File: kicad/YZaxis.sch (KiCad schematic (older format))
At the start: 34 parts, among them CON16 YZ, CON17 Stepstick_Left_Connector, CON18 Stepstick_Right_Connector, CON19 Stepstick_Left_Connector, CON20 Stepstick_Right_Connector, Q5 IRLR2905ZPBF, Q6 FDC6401N, U1 CD4504BPW

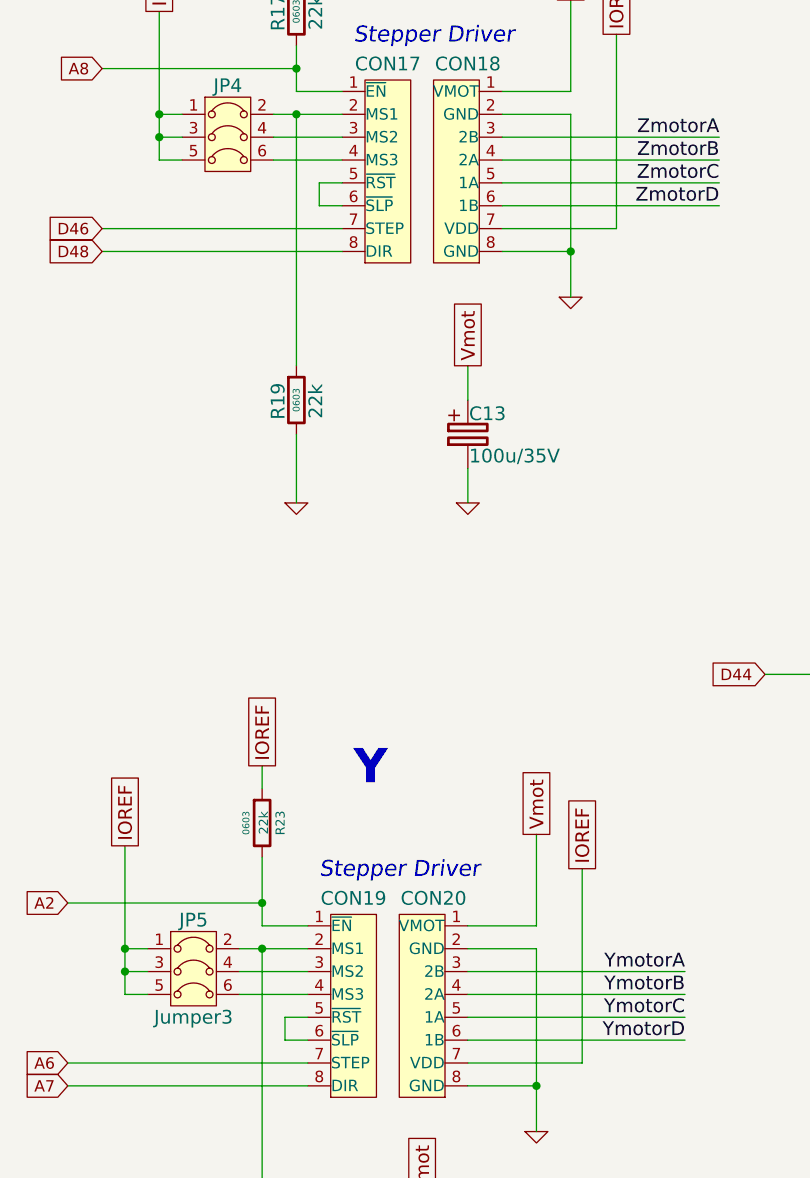
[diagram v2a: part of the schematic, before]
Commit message: Add footprint informations
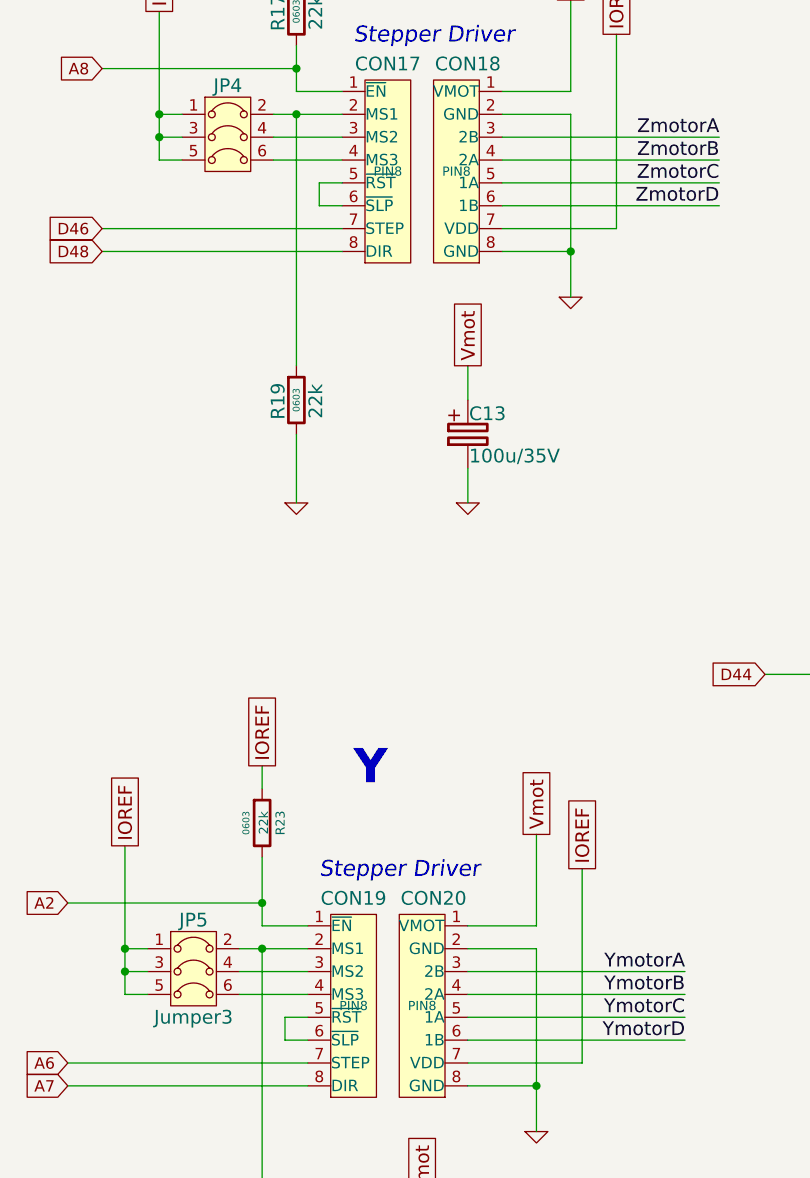
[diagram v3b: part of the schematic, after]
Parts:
- CON17, CON18, CON19, CON20: footprint (none) -> PIN8
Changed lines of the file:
@@
 F 0 "CON19" H 2400 6170 60  0000 C CNN
 F 1 "Stepstick_Left_Connector" H 2400 5250 60  0001 C CNN
-F 2 "" H 2400 5700 40  0000 C CNN
+F 2 "PIN8" H 2400 5700 40  0000 C CNN
 F 3 "" H 2400 5700 40  0000 C CNN
 	1    2400 5700
@@
 F 0 "CON20" H 2750 6170 60  0000 C CNN
 F 1 "Stepstick_Right_Connector" H 2750 5250 60  0001 C CNN
-F 2 "" H 2700 5700 40  0000 C CNN
+F 2 "PIN8" H 2700 5700 40  0000 C CNN
 F 3 "" H 2700 5700 40  0000 C CNN
 	1    2750 5700
@@
 F 0 "CON17" H 2550 2520 60  0000 C CNN
 F 1 "Stepstick_Left_Connector" H 2550 1600 60  0001 C CNN
-F 2 "" H 2550 2050 40  0000 C CNN
+F 2 "PIN8" H 2550 2050 40  0000 C CNN
 F 3 "" H 2550 2050 40  0000 C CNN
 	1    2550 2050
@@
 F 0 "CON18" H 2900 2520 60  0000 C CNN
 F 1 "Stepstick_Right_Connector" H 2900 1600 60  0001 C CNN
-F 2 "" H 2850 2050 40  0000 C CNN
+F 2 "PIN8" H 2850 2050 40  0000 C CNN
 F 3 "" H 2850 2050 40  0000 C CNN
 	1    2900 2050

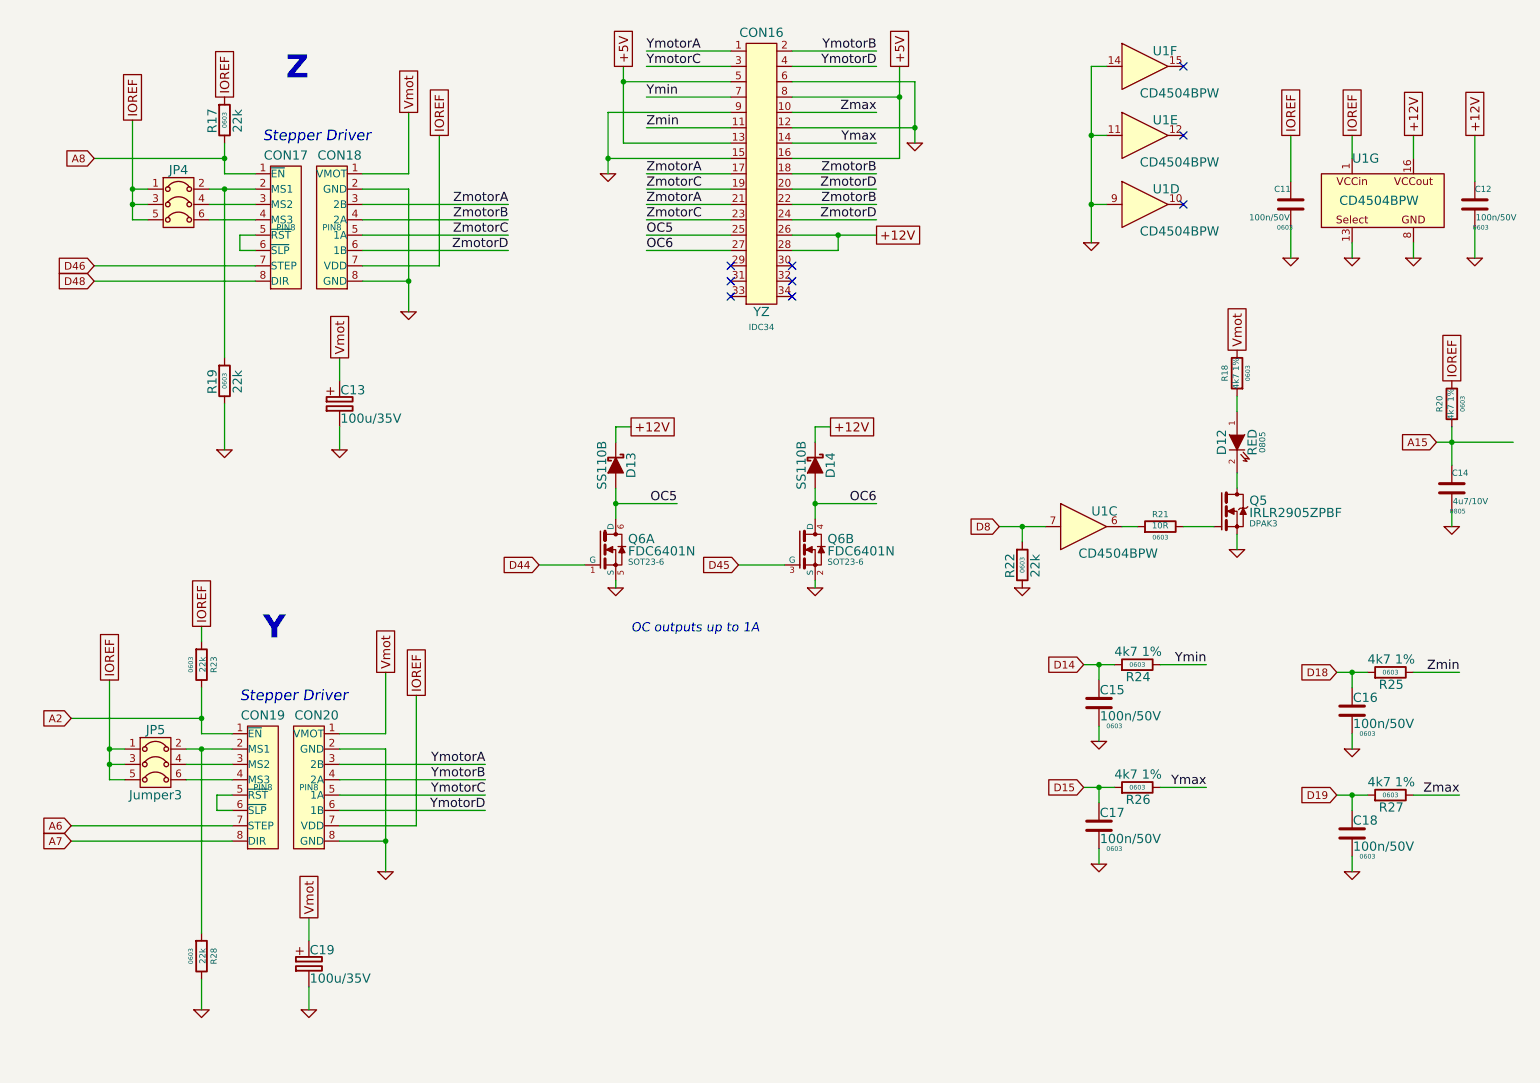
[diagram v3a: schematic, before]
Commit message: Add footprint informations
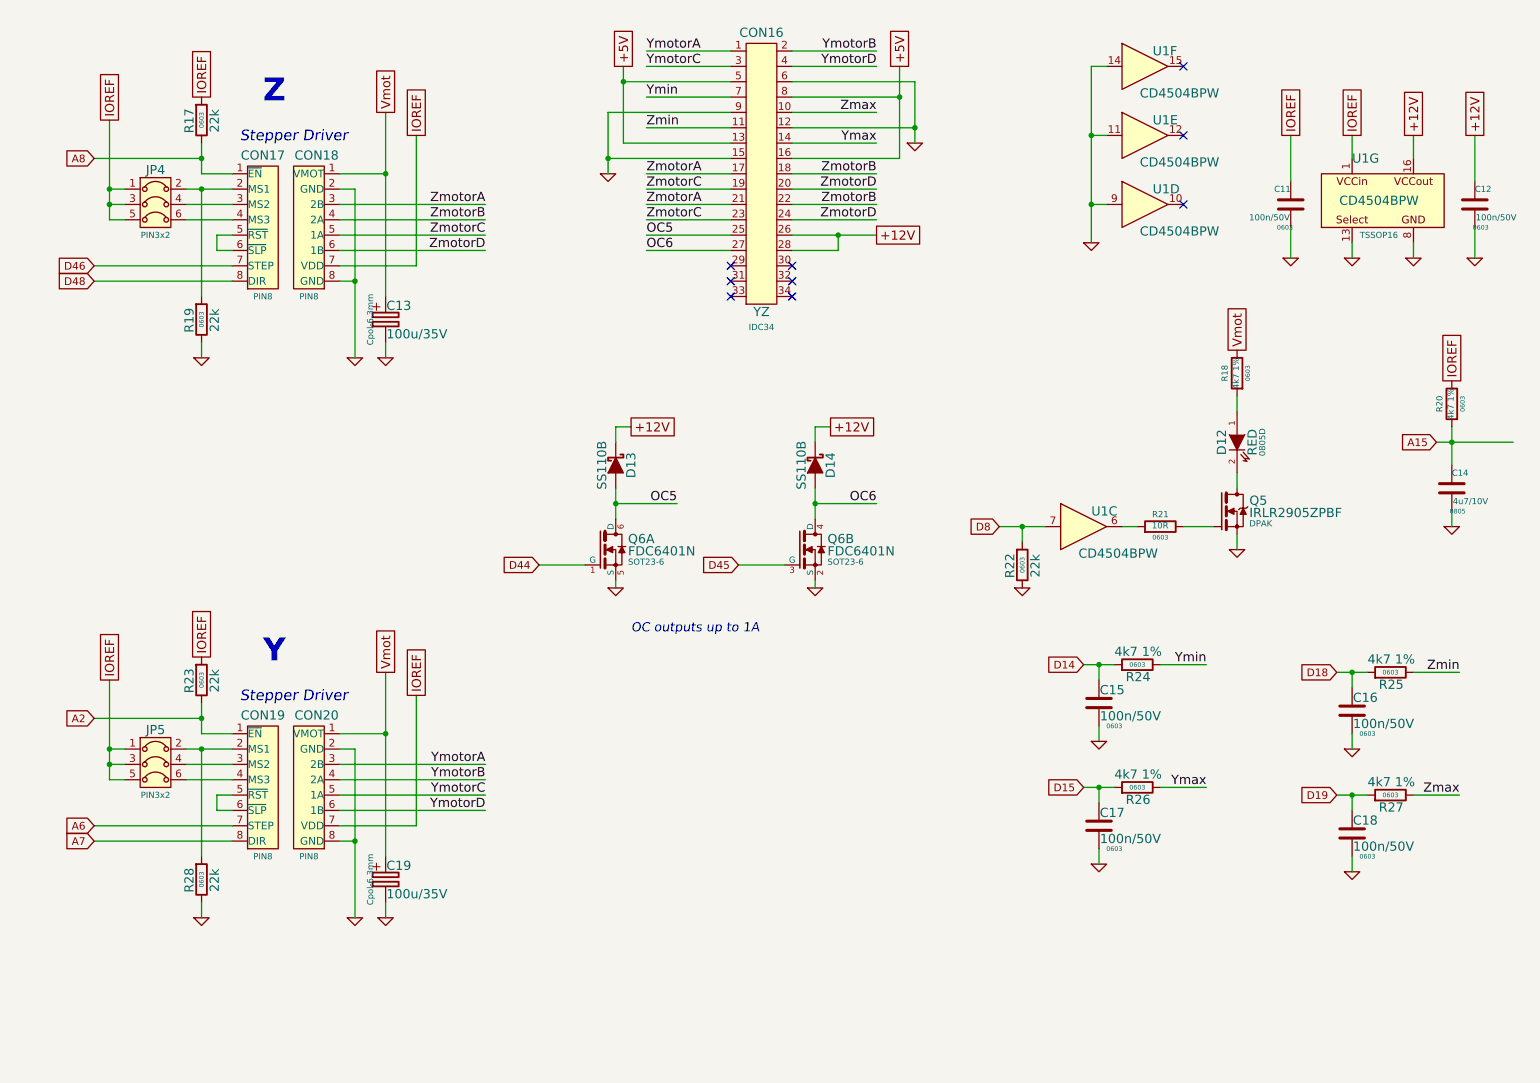
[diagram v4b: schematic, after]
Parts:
- C13, C19: footprint (none) -> Cpol-6.3mm
- D12: footprint 0805 -> 0805D
- JP4, JP5: footprint (none) -> PIN3x2
- Q5: footprint DPAK3 -> DPAK
